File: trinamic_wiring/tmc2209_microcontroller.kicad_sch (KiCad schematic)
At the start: 3 parts, among them M4 Stepper_Motor_QSH2818-32-07-0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

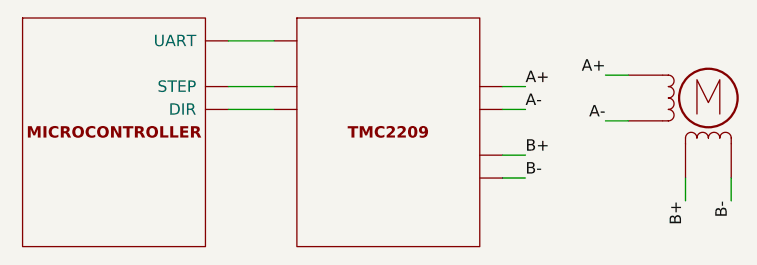
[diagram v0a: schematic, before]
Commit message: Remove unused sheets
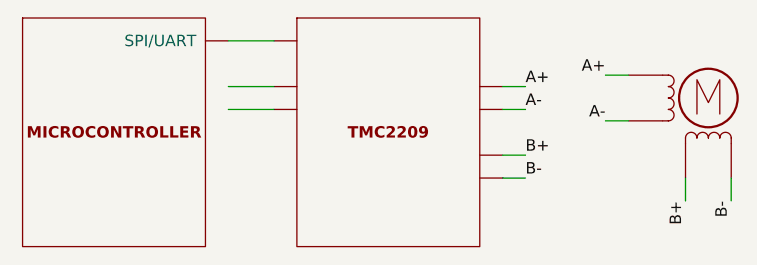
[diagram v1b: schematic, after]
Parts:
- TMC14: value DOC_TMC2209 -> TMC2209_DOC; symbol Janelia:DOC_TMC2209 -> Janelia:TMC2209_DOC
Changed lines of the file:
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@@
   (title_block
     (title "Trinamic Wiring")
-    (date "2023-08-02")
+    (date "2024-01-31")
     (rev "0.4")
     (company "Janelia Research Campus")
@@
           (reference "M4") (unit 1)
         )
-        (path "/e4144788-6304-493f-818e-5d881d3b7418/a161638e-a96f-4455-865a-1d7502675f43/8b14fa14-b5a5-4a20-b7f5-9504bcb63f71"
-          (reference "M4") (unit 1)
-        )
       )
     )
   )
-  (symbol (lib_id "Janelia:DOC_TMC2209") (at 134.62 91.44 0) (unit 1)
+  (symbol (lib_id "Janelia:TMC2209_DOC") (at 134.62 91.44 0) (unit 1)
     (in_bom yes) (on_board yes) (dnp no) (fields_autoplaced)
     (property "Reference" "TMC14" (at 134.62 72.39 0)
       (effects (font (size 1.27 1.27)) hide)
     )
-    (property "Value" "DOC_TMC2209" (at 134.62 77.47 0)
+    (property "Value" "TMC2209_DOC" (at 134.62 77.47 0)
       (effects (font (size 1.524 1.524)) hide)
     )
@@
       (project "trinamic_wiring"
         (path "/e4144788-6304-493f-818e-5d881d3b7418/c8eda2b5-ab13-4033-82d9-875c9fcaf884/8b14fa14-b5a5-4a20-b7f5-9504bcb63f71"
-          (reference "TMC14") (unit 1)
-        )
-        (path "/e4144788-6304-493f-818e-5d881d3b7418/a161638e-a96f-4455-865a-1d7502675f43/8b14fa14-b5a5-4a20-b7f5-9504bcb63f71"
           (reference "TMC14") (unit 1)
         )
@@
           (reference "MICROCONTROLLER8") (unit 1)
         )
-        (path "/e4144788-6304-493f-818e-5d881d3b7418/a161638e-a96f-4455-865a-1d7502675f43/8b14fa14-b5a5-4a20-b7f5-9504bcb63f71"
-          (reference "MICROCONTROLLER8") (unit 1)
-        )
